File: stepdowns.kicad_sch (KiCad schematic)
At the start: 66 parts, among them J1 12V OUTLET, J2 5V OUTLET, J3 3V3 OUTLET, J4 PWRBTN, J5 PWRONOUT, Q1 BSS138, Q2 BSS138, U1 XL7005A, U2 VIPER115LS, U3 LM1117-3.3, U9 LTV-817S

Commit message: Fixes, layouting
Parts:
- removed TP2: 3V3, TestPoint:TestPoint_Pad_D2.0mm, symbol Connector:TestPoint
- removed U9: LTV-817S, Package_DIP:SMDIP-4_W9.53mm, symbol Isolator:LTV-817S
- added U9: TLP291, Package_SO:SOIC-4_4.55x2.6mm_P1.27mm, symbol Isolator:TLP291
- C23, C24, C25: value 10uF -> 0.1uF
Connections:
- net GND: now also U9.2
- net at R54.2: now also U9.1
- net at J5.2 (Pin_2): now also U9.3
- net at J5.1 (Pin_1): now also U9.4
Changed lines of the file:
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@@
   (junction (at 111.76 58.42) (diameter 0) (color 0 0 0 0)
   )
-  (junction (at 251.46 69.85) (diameter 0) (color 0 0 0 0)
-  )
   (junction (at 194.31 114.3) (diameter 0) (color 0 0 0 0)
   )
@@
     (stroke (width 0) (type default))
   )
-  (wire (pts (xy 251.46 67.31) (xy 251.46 69.85))
-    (stroke (width 0) (type default))
-  )
   (wire (pts (xy 162.56 168.91) (xy 160.02 168.91))
     (stroke (width 0) (type default))
@@
     (stroke (width 0) (type default))
   )
-  (wire (pts (xy 243.84 69.85) (xy 251.46 69.85))
-    (stroke (width 0) (type default))
-  )
   (wire (pts (xy 224.79 114.3) (xy 228.6 114.3))
     (stroke (width 0) (type default))
@@
     (stroke (width 0) (type default))
   )
-  (wire (pts (xy 251.46 69.85) (xy 257.81 69.85))
+  (wire (pts (xy 243.84 69.85) (xy 257.81 69.85))
     (stroke (width 0) (type default))
   )
@@
       (effects (font (size 1.27 1.27)) (justify left))
     )
-    (property "Value" "10uF" (at 236.22 144.78 0)
+    (property "Value" "0.1uF" (at 236.22 144.78 0)
       (effects (font (size 1.27 1.27)) (justify left))
     )
@@
     )
   )
+  (symbol (lib_id "Isolator:TLP291") (at 149.86 170.18 0) (unit 1)
+    (in_bom yes) (on_board yes) (dnp no) (fields_autoplaced)
+    (property "Reference" "U9" (at 149.86 161.29 0)
+      (effects (font (size 1.27 1.27)))
+    )
+    (property "Value" "TLP291" (at 149.86 163.83 0)
+      (effects (font (size 1.27 1.27)))
+    )
+    (property "Footprint" "Package_SO:SOIC-4_4.55x2.6mm_P1.27mm" (at 144.78 175.26 0)
+      (effects (font (size 1.27 1.27) italic) (justify left) hide)
+    )
+    (property "Datasheet" "https://toshiba.semicon-storage.com/info/docget.jsp?did=12884&prodName=TLP291" (at 149.86 170.18 0)
+      (effects (font (size 1.27 1.27)) (justify left) hide)
+    )
+    (pin "1")
+    (pin "3")
+    (pin "2")
+    (pin "4")
+    (instances
+      (project "ShiftWay_f103"
+        (path "/c57bc97c-1c43-4bb1-9424-fed846030b7b/38230a7e-96be-4145-8fae-a896a24d853d"
+          (reference "U9") (unit 1)
+        )
+      )
+    )
+  )
   (symbol (lib_id "4shift:VIPER115LSTR") (at 91.44 58.42 180) (unit 1)
     (in_bom yes) (on_board yes) (dnp no)
@@
       (effects (font (size 1.27 1.27)) (justify left))
     )
-    (property "Value" "10uF" (at 246.38 144.78 0)
+    (property "Value" "0.1uF" (at 246.38 144.78 0)
       (effects (font (size 1.27 1.27)) (justify left))
     )
@@
     )
   )
-  (symbol (lib_id "Isolator:LTV-817S") (at 149.86 170.18 0) (unit 1)
-    (in_bom yes) (on_board yes) (dnp no) (fields_autoplaced)
-    (property "Reference" "U9" (at 149.86 161.29 0)
-      (effects (font (size 1.27 1.27)))
-    )
-    (property "Value" "LTV-817S" (at 149.86 163.83 0)
-      (effects (font (size 1.27 1.27)))
-    )
-    (property "Footprint" "Package_DIP:SMDIP-4_W9.53mm" (at 149.86 177.8 0)
-      (effects (font (size 1.27 1.27)) hide)
-    )
-    (property "Datasheet" "http://www.us.liteon.com/downloads/LTV-817-827-847.PDF" (at 140.97 162.56 0)
-      (effects (font (size 1.27 1.27)) hide)
-    )
-    (pin "3")
-    (pin "2")
-    (pin "1")
-    (pin "4")
-    (instances
-      (project "ShiftWay_f103"
-        (path "/c57bc97c-1c43-4bb1-9424-fed846030b7b/38230a7e-96be-4145-8fae-a896a24d853d"
-          (reference "U9") (unit 1)
-        )
-      )
-    )
-  )
   (symbol (lib_id "Connector:TestPoint") (at 228.6 106.68 0) (unit 1)
     (in_bom yes) (on_board yes) (dnp no) (fields_autoplaced)
@@
     )
   )
-  (symbol (lib_id "Connector:TestPoint") (at 251.46 67.31 0) (unit 1)
-    (in_bom yes) (on_board yes) (dnp no) (fields_autoplaced)
-    (property "Reference" "TP2" (at 252.857 62.7959 0)
-      (effects (font (size 1.27 1.27)) (justify left))
-    )
-    (property "Value" "3V3" (at 252.857 65.2201 0)
-      (effects (font (size 1.27 1.27)) (justify left))
-    )
-    (property "Footprint" "TestPoint:TestPoint_Pad_D2.0mm" (at 256.54 67.31 0)
-      (effects (font (size 1.27 1.27)) hide)
-    )
-    (property "Datasheet" "~" (at 256.54 67.31 0)
-      (effects (font (size 1.27 1.27)) hide)
-    )
-    (pin "1")
-    (instances
-      (project "ShiftWay_f103"
-        (path "/c57bc97c-1c43-4bb1-9424-fed846030b7b/38230a7e-96be-4145-8fae-a896a24d853d"
-          (reference "TP2") (unit 1)
-        )
-      )
-    )
-  )
   (symbol (lib_id "power:+3V3") (at 259.08 106.68 90) (unit 1)
     (in_bom yes) (on_board yes) (dnp no) (fields_autoplaced)
@@
       (effects (font (size 1.27 1.27)) (justify left))
     )
-    (property "Value" "10uF" (at 256.54 144.78 0)
+    (property "Value" "0.1uF" (at 256.54 144.78 0)
       (effects (font (size 1.27 1.27)) (justify left))
     )

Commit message: removed swd
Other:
- moved on the sheet: D7, R10, R9

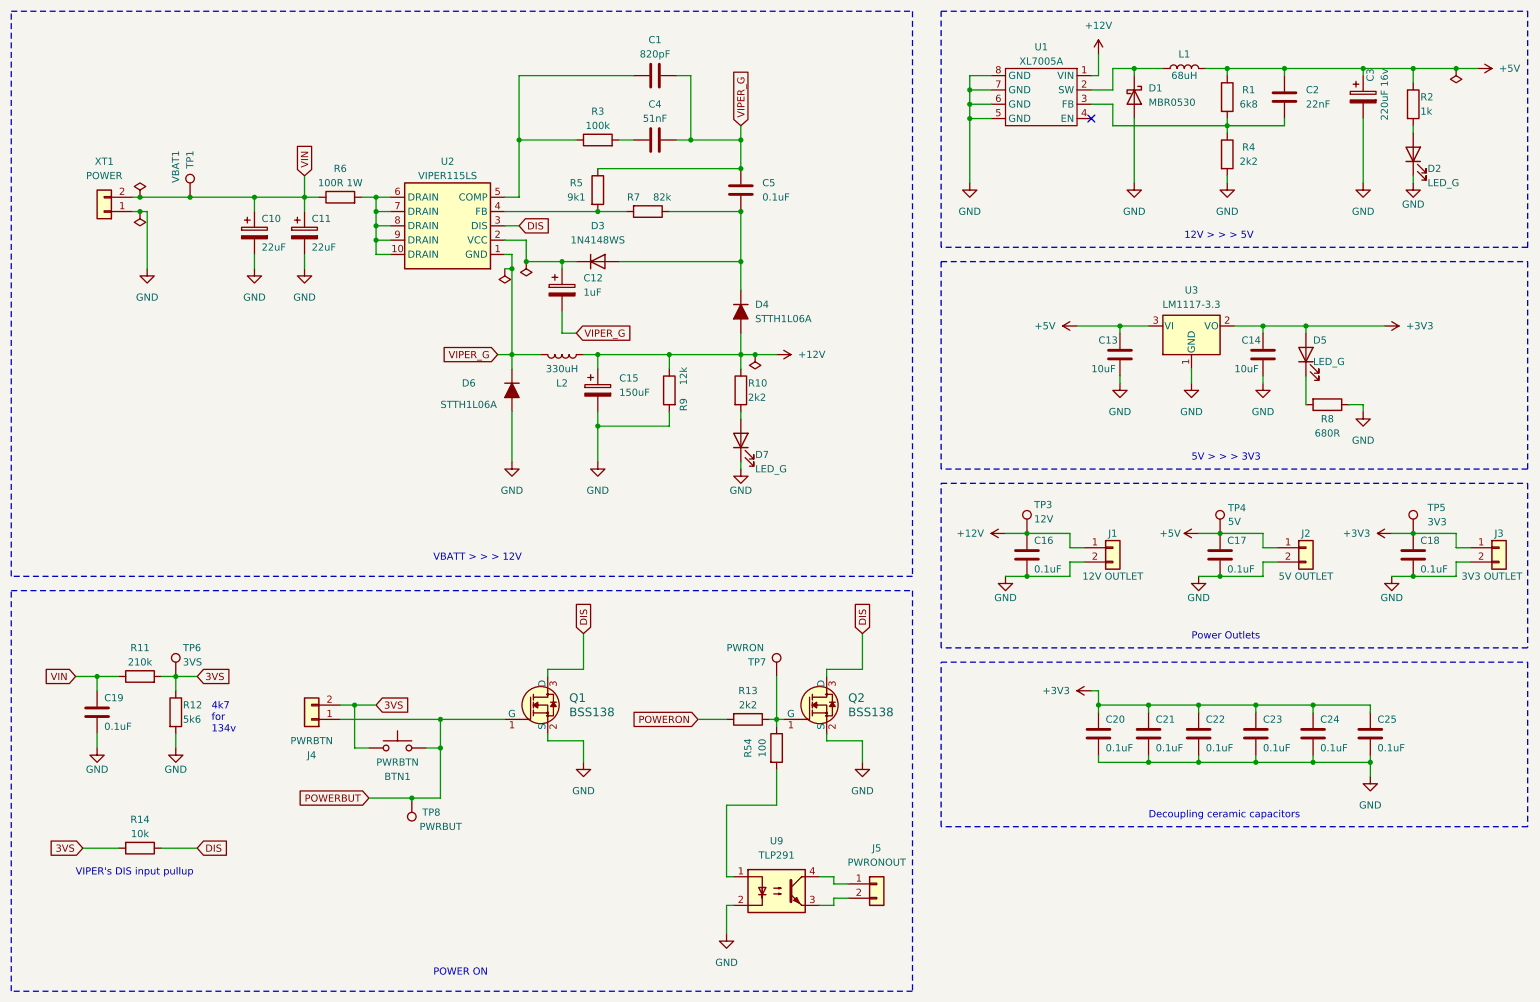
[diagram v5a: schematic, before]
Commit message: Major update on results of testing first order board and on results of crosscheck
* reworked mainswitch scheme
* mainswitch divider. expected commutation time - 2us
* added 3v3bt and 3v3hall
* tvs on hall
* divided 5vhall, 3vhall, 3vbt
* fix misplacement gnd and 3v3 at the BT connector
* fix motorbut (now pullup and gnd on button)
* fix opto gate

+ a lot of minors
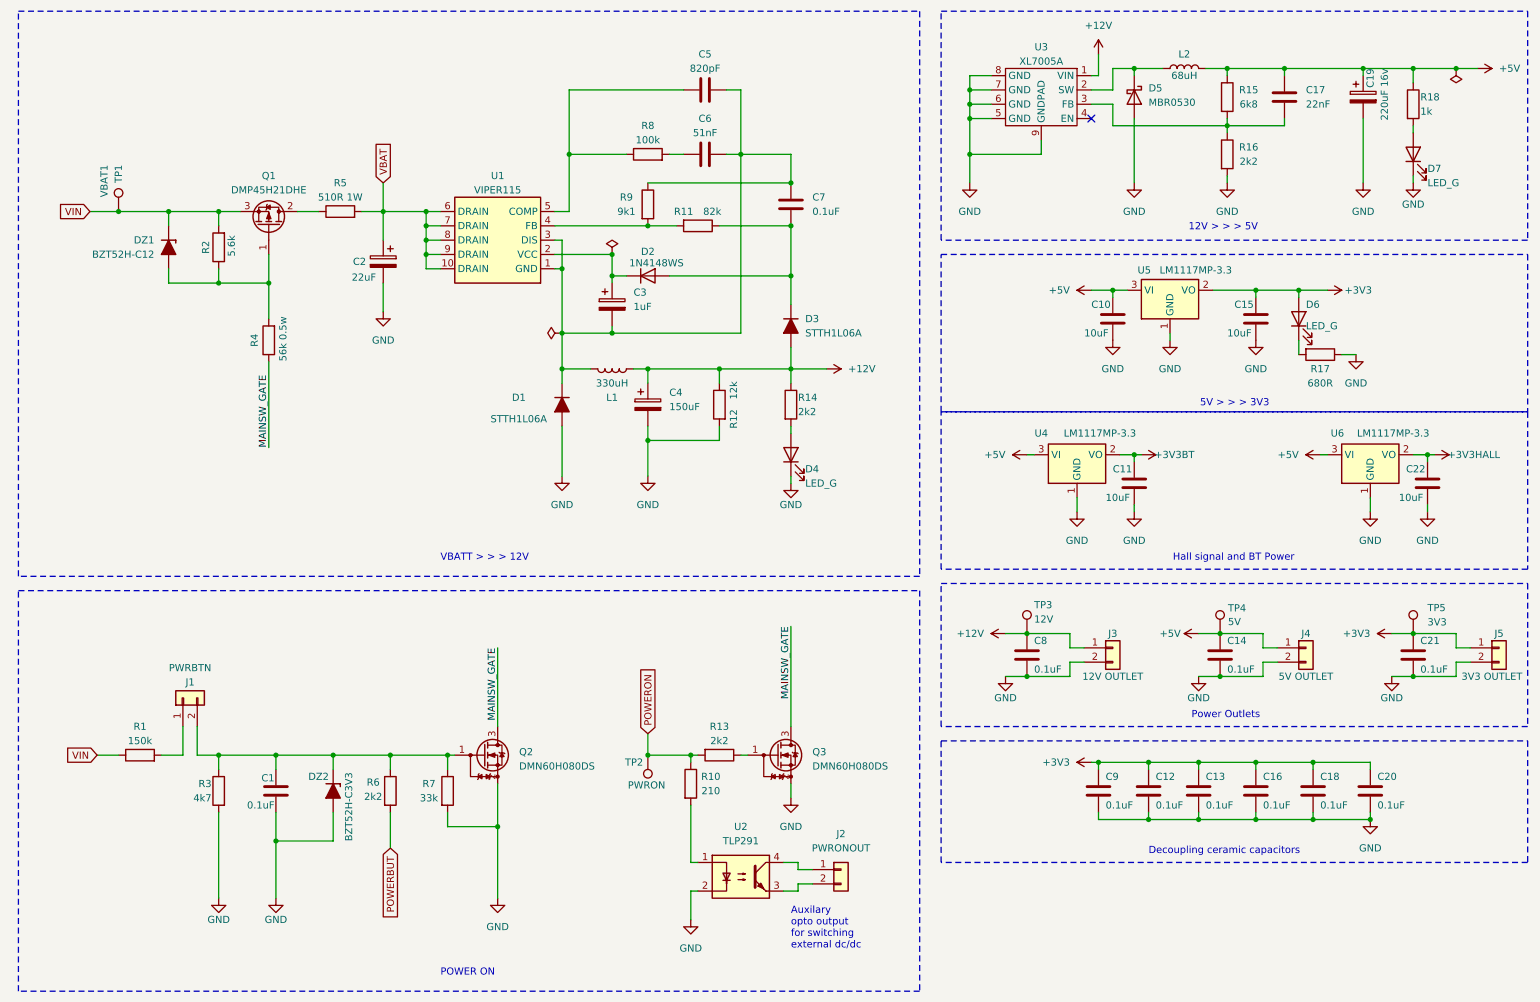
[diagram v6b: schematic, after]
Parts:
- removed BTN1: PWRBTN, Button_Switch_SMD:SW_SPST_SKQG_WithoutStem, symbol Switch:SW_Push
- removed C10, C11: 22uF, Capacitor_SMD:CP_Elec_10x10, symbol Device:C_Polarized
- removed C12: 1uF, Capacitor_SMD:CP_Elec_10x10, symbol Device:C_Polarized
- removed C15: 150uF, Capacitor_SMD:CP_Elec_10x10, symbol Device:C_Polarized
- removed C19: 0.1uF, Capacitor_SMD:C_0805_2012Metric_Pad1.18x1.45mm_HandSolder, symbol Device:C
- removed C4: 51nF, Capacitor_SMD:C_0603_1608Metric_Pad1.08x0.95mm_HandSolder, symbol Device:C
- removed D3: 1N4148WS, Diode_SMD:D_SOD-323, symbol Diode:1N4148WS
- removed D4, D6: STTH1L06A, Diode_SMD:D_SMA_Handsoldering, symbol PCM_Diode_AKL:STTH1L06A
- removed D7: LED_G, LED_SMD:LED_0603_1608Metric, symbol Device:LED
- removed J4: PWRBTN, Connector_JST:JST_XH_B2B-XH-A_1x02_P2.50mm_Vertical, symbol Connector_Generic:Conn_01x02
- removed J5: PWRONOUT, Connector_JST:JST_XH_B2B-XH-A_1x02_P2.50mm_Vertical, symbol Connector_Generic:Conn_01x02
- removed L2: 330uH, Inductor_SMD:L_Bourns_SRR1208_12.7x12.7mm, symbol Device:L
- removed Q1, Q2: BSS138, digikey-footprints:SOT-23-3, symbol dk_Transistors-FETs-MOSFETs-Single:BSS138
- removed R54: 100, Resistor_SMD:R_0603_1608Metric_Pad0.98x0.95mm_HandSolder, symbol Device:R
- removed TP6: 3VS, TestPoint:TestPoint_Pad_D2.0mm, symbol Connector:TestPoint
- removed TP7: PWRON, TestPoint:TestPoint_Pad_D2.0mm, symbol Connector:TestPoint
- removed TP8: PWRBUT, TestPoint:TestPoint_Pad_D2.0mm, symbol Connector:TestPoint
- removed U2: VIPER115LS, 4shift:SOIC100P600X175-10N, symbol 4shift:VIPER115LSTR
- removed U9: TLP291, Package_SO:SOIC-4_4.55x2.6mm_P1.27mm, symbol Isolator:TLP291
- removed XT1: POWER, Connector_AMASS:AMASS_XT30PW-M_1x02_P2.50mm_Horizontal, symbol Connector_Generic:Conn_01x02
- added C11, C22: 10uF, Capacitor_SMD:C_0603_1608Metric_Pad1.08x0.95mm_HandSolder, symbol Device:C
- added C2: 22uF, symbol Device:C_Polarized
- added C3: 1uF, Capacitor_SMD:CP_Elec_10x10, symbol Device:C_Polarized
- added C4: 150uF, Capacitor_SMD:CP_Elec_10x10, symbol Device:C_Polarized
- added C6: 51nF, Capacitor_SMD:C_0603_1608Metric, symbol Device:C
- added C7: 0.1uF, Capacitor_SMD:C_0603_1608Metric, symbol Device:C
- added D1, D3: STTH1L06A, Diode_SMD_AKL:D_SMA, symbol Diode_AKL:STTH1L06A
- added D2: 1N4148WS, Diode_SMD:D_SOD-323, symbol Diode:1N4148WS
- added D4: LED_G, LED_SMD:LED_0603_1608Metric, symbol Device:LED
- added DZ1: BZT52H-C12, Diode_SMD_AKL:D_SOD-123F, symbol Diode_Zener_AKL:BZT52H-C12
- added DZ2: BZT52H-C3V3, Diode_SMD_AKL:D_SOD-123F, symbol Diode_Zener_AKL:BZT52H-C3V3
- added J1: PWRBTN, Connector_JST:JST_XH_B2B-XH-A_1x02_P2.50mm_Vertical, symbol Connector_Generic:Conn_01x02
- added J2: PWRONOUT, Connector_JST:JST_XH_B2B-XH-A_1x02_P2.50mm_Vertical, symbol Connector_Generic:Conn_01x02
- added L1: 330uH, Inductor_SMD:L_Bourns_SRR1208_12.7x12.7mm, symbol Device:L
- added Q1: DMP45H21DHE, Package_TO_SOT_SMD:SOT-223-3_TabPin2, symbol 4shift:DMP45H21DHE
- added Q2, Q3: DMN60H080DS, Package_TO_SOT_SMD:SOT-23, symbol Transistor_FET:DMN60H080DS
- added R1: 150k, Resistor_SMD:R_0805_2012Metric, symbol Device:R
- added R2: 5.6k, Resistor_SMD:R_0805_2012Metric, symbol Device:R
- added R4: 56k 0.5w, Resistor_SMD:R_0805_2012Metric, symbol Device:R
- added R8: 100k, Resistor_SMD:R_0603_1608Metric, symbol Device:R
- added TP2: PWRON, TestPoint:TestPoint_Pad_D2.0mm, symbol Connector:TestPoint
- added U1: VIPER115, tollshift:SOIC100P600X175-10N, symbol tollshift:VIPER115LSTR
- added U2: TLP291, Package_SO:SOIC-4_4.55x2.6mm_P1.27mm, symbol Isolator:TLP291
- added U4, U6: LM1117MP-3.3, Package_TO_SOT_SMD:SOT-223-3_TabPin2, symbol Regulator_Linear:LM1117MP-3.3
- C1: value 820pF -> 0.1uF; footprint Capacitor_SMD:C_0603_1608Metric_Pad1.08x0.95mm_HandSolder -> Capacitor_SMD:C_0805_2012Metric
- C5: value 0.1uF -> 820pF; footprint Capacitor_SMD:C_0603_1608Metric_Pad1.08x0.95mm_HandSolder -> Capacitor_SMD:C_0603_1608Metric
- R10: value 2k2 -> 210; footprint Resistor_SMD:R_0603_1608Metric_Pad0.98x0.95mm_HandSolder -> Resistor_SMD:R_0603_1608Metric
- R11: value 210k -> 82k; footprint Resistor_SMD:R_0805_2012Metric_Pad1.20x1.40mm_HandSolder -> Resistor_SMD:R_0603_1608Metric
- R12: value 5k6 -> 12k; footprint Resistor_SMD:R_0805_2012Metric_Pad1.20x1.40mm_HandSolder -> Resistor_SMD:R_0603_1608Metric
- R13: footprint Resistor_SMD:R_0603_1608Metric_Pad0.98x0.95mm_HandSolder -> Resistor_SMD:R_0603_1608Metric
- R14: value 10k -> 2k2; footprint Resistor_SMD:R_0603_1608Metric_Pad0.98x0.95mm_HandSolder -> Resistor_SMD:R_0603_1608Metric
- R3: value 100k -> 4k7; footprint Resistor_SMD:R_0603_1608Metric_Pad0.98x0.95mm_HandSolder -> Resistor_SMD:R_0805_2012Metric
- R5: value 9k1 -> 510R 1W; footprint Resistor_SMD:R_0603_1608Metric_Pad0.98x0.95mm_HandSolder -> Resistor_SMD:R_2010_5025Metric
- R6: value 100R 1W -> 2k2; footprint Resistor_SMD:R_2010_5025Metric_Pad1.40x2.65mm_HandSolder -> Resistor_SMD:R_0603_1608Metric
- R7: value 82k -> 33k; footprint Resistor_SMD:R_0603_1608Metric_Pad0.98x0.95mm_HandSolder -> Resistor_SMD:R_0603_1608Metric
- R9: value 12k -> 9k1; footprint Resistor_SMD:R_0603_1608Metric_Pad0.98x0.95mm_HandSolder -> Resistor_SMD:R_0603_1608Metric
- U5: renamed from U3; value LM1117-3.3 -> LM1117MP-3.3; footprint Package_TO_SOT_SMD:SOT-223 -> Package_TO_SOT_SMD:SOT-223-3_TabPin2; symbol Regulator_Linear:LM1117-3.3 -> Regulator_Linear:LM1117MP-3.3
- renumbered C13 to C10, C21 to C12, C22 to C13, C17 to C14, C14 to C15, C23 to C16, C2 to C17, C24 to C18, C3 to C19, C25 to C20, C18 to C21, C16 to C8, C20 to C9, D1 to D5, D5 to D6, D2 to D7, J1 to J3, J2 to J4, J3 to J5, L1 to L2, R1 to R15, R4 to R16, R8 to R17, R2 to R18, U1 to U3
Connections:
- net DIS is gone; now on net +12V: R14.1
- net +12V: now also R12.1, C4.1, D3.2 (A), L1.2; no longer R10.1, R9.1
- net +5V: now also U4.3 (VI), U6.3 (VI)
- net GND: now also C1.2, R3.2, R7.2, U3.9 (GNDPAD), C11.2, C2.2, C22.2, C4.2, D1.2 (A), D4.1 (K), DZ2.2 (A), Q2.2 (S), Q3.2 (S), U2.2, U4.1 (GND), U6.1 (GND); no longer R9.2
- net POWERBUT: now also R6.2
- net POWERON: now also R10.1, TP2.1
- net VIN: now also DZ1.1 (K), Q1.3 (S), R1.1, R2.2; no longer R11.1, R6.1
- net at R10.2: now also U2.1
- net at R13.1: now also Q3.1 (G)
- net VBAT: now reaches R5.2
- net VBAT: now also C2.1, U1.10 (DRAIN), U1.6 (DRAIN), U1.7 (DRAIN), U1.8 (DRAIN), U1.9 (DRAIN); no longer R7.2
- net at C1.1, R3.1: now also R6.1, R7.1, DZ2.1 (K), J1.2 (Pin_2), Q2.1 (G)
- net at C5.1: now also R8.1, U1.5 (COMP); no longer R7.1
- removed net 3VS: R11.2, R12.1, R14.2
- removed net VIPER_G: C1.2, C5.2, R5.1
- new net: C7.1, D2.2 (A), D3.1 (K), R11.1
- new net: J2.1 (Pin_1), U2.4
- new net: J2.2 (Pin_2), U2.3
- new net: C6.1, R8.2
- new net: C3.2, C5.2, C6.2, C7.2, D1.1 (K), L1.1, R9.1, U1.1 (GND), U1.3 (DIS)
- new net: R11.2, R9.2, U1.4 (FB)
- new net: J1.1 (Pin_1), R1.2
- new net: DZ1.2 (A), Q1.1 (G), R2.1, R4.2
- new net: C3.1, D2.1 (K), U1.2 (VCC)
- new net: D4.2 (A), R14.2
- new net: Q1.2 (D), R5.1
- new net +3V3BT: C11.1, U4.2 (VO)
- new net +3V3HALL: C22.1, U6.2 (VO)
- new net MAINSW_GATE: Q2.3 (D), Q3.3 (D), R4.1
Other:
- note added: "Auxilary opto output for switching external dc/dc"
- note added: "Hall signal and BT Power"
- note removed: "4k7 for 134v"
- note removed: "VIPER's DIS input pullup"
- moved on the sheet: C10, C12, C13, C14, C15, C16, C18, C20, C21, C8, C9, D6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

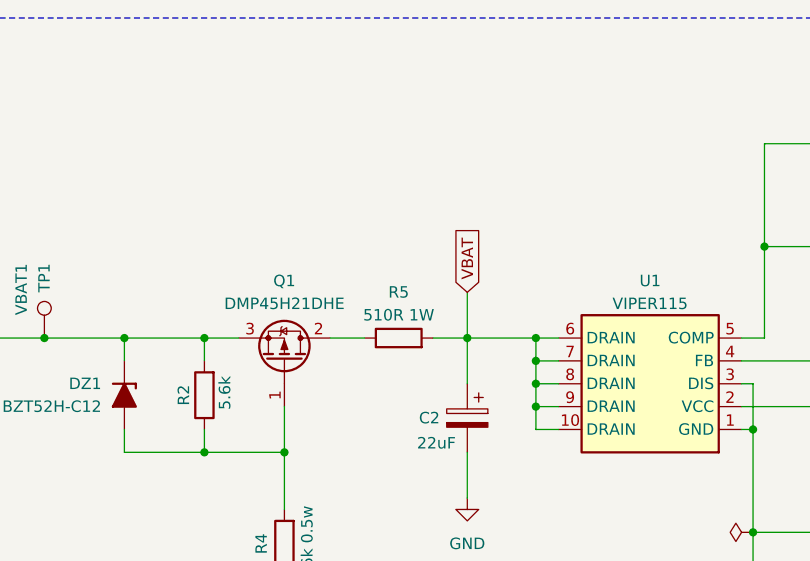
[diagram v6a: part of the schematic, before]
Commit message: Fix pullup IMU, pulldown boot0, vbat before resi
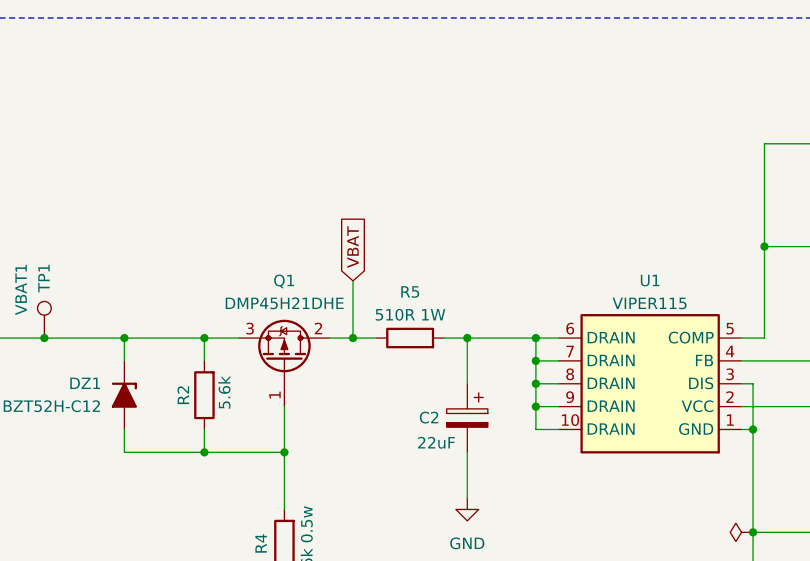
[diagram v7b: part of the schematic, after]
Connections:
- net VBAT: now also Q1.2 (D), R5.1; no longer C2.1, R5.2, U1.10 (DRAIN), U1.6 (DRAIN), U1.7 (DRAIN), U1.8 (DRAIN), U1.9 (DRAIN)
- new net: C2.1, R5.2, U1.10 (DRAIN), U1.6 (DRAIN), U1.7 (DRAIN), U1.8 (DRAIN), U1.9 (DRAIN)
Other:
- moved on the sheet: R5
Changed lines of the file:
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@@
 	)
 	(junction
+		(at 67.31 49.53)
+		(diameter 0)
+		(color 0 0 0 0)
+	)
+	(junction
 		(at 228.6 132.08)
 		(diameter 0)
@@
 	(wire
 		(pts
+			(xy 67.31 49.53) (xy 69.85 49.53)
+		)
+		(stroke
+			(width 0)
+			(type default)
+		)
+	)
+	(wire
+		(pts
 			(xy 259.08 124.46) (xy 262.89 124.46)
 		)
@@
 	(wire
 		(pts
-			(xy 76.2 49.53) (xy 80.01 49.53)
-		)
-		(stroke
-			(width 0)
-			(type default)
-		)
-	)
-	(wire
-		(pts
 			(xy 41.91 59.69) (xy 41.91 62.23)
 		)
@@
 	(wire
 		(pts
-			(xy 64.77 49.53) (xy 68.58 49.53)
+			(xy 64.77 49.53) (xy 67.31 49.53)
 		)
 		(stroke
@@
 	(wire
 		(pts
+			(xy 67.31 43.18) (xy 67.31 49.53)
+		)
+		(stroke
+			(width 0)
+			(type default)
+		)
+	)
+	(wire
+		(pts
 			(xy 143.51 39.37) (xy 143.51 27.94)
 		)
@@
 	(wire
 		(pts
+			(xy 77.47 49.53) (xy 80.01 49.53)
+		)
+		(stroke
+			(width 0)
+			(type default)
+		)
+	)
+	(wire
+		(pts
 			(xy 240.03 24.13) (xy 254 24.13)
 		)
@@
 	(wire
 		(pts
-			(xy 80.01 44.45) (xy 80.01 49.53)
-		)
-		(stroke
-			(width 0)
-			(type default)
-		)
-	)
-	(wire
-		(pts
 			(xy 81.28 146.05) (xy 91.44 146.05)
 		)
@@
 	(global_label "VBAT"
 		(shape input)
-		(at 80.01 44.45 90)
+		(at 67.31 43.18 90)
 		(fields_autoplaced yes)
 		(effects
@@
 		)
 		(property "Intersheetrefs" "${INTERSHEET_REFS}"
-			(at 80.01 37.05 90)
+			(at 67.31 35.78 90)
 			(effects
 				(font
@@
 	(symbol
 		(lib_id "Device:R")
-		(at 72.39 49.53 90)
+		(at 73.66 49.53 90)
 		(unit 1)
 		(exclude_from_sim no)
@@
 		(dnp no)
 		(property "Reference" "R5"
-			(at 72.39 44.45 90)
+			(at 73.66 44.45 90)
 			(effects
 				(font
@@
 		)
 		(property "Value" "510R 1W"
-			(at 72.39 46.99 90)
+			(at 73.66 46.99 90)
 			(effects
 				(font
@@
 		)
 		(property "Footprint" "Resistor_SMD:R_2010_5025Metric"
-			(at 72.39 51.308 90)
+			(at 73.66 51.308 90)
 			(effects
 				(font
@@
 		)
 		(property "Datasheet" "~"
-			(at 72.39 49.53 0)
+			(at 73.66 49.53 0)
 			(effects
 				(font
@@
 		)
 		(property "Description" ""
-			(at 72.39 49.53 0)
+			(at 73.66 49.53 0)
 			(effects
 				(font
